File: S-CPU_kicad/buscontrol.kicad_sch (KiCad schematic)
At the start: 123 parts, among them U6 MUX, U8 MUX

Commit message: Fix ERC errors in schematics.
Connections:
- removed net 65816_?: LBOQ.3, MAWW.3, U6.4, U8.4
- net wIAYI renamed wIAYI_~{RST}
- net wJBDJ renamed CPU_~{RST}
- new net 65816_IN0: LBOQ.3
- new net 65816_IN1: MAWW.3
- new net 65816_PHI2: U8.4
- new net 65816_~{RST}: U6.4
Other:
- title: SNES S-CPU Schematics  -> Reverse Engineered SNES S-CPU Schematics 

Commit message: Big rework on the hierachical sheet to make thigs a bit clearer. PDF exported for Rev 0.1.
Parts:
- removed DCEG, FBSI: TRI_INV_IF2, symbol Ricoh_Cells:TRI_INV_IF2
- removed GBEG, IARF: OR_3, symbol Ricoh_Cells:OR_3
- removed HAKW, IBEP, JBDJ, JBQK, MBSK: BUF, symbol Ricoh_Cells:BUF
- removed HALC, HBCT, HBGA, IAQU, IBGG, KBVA, LBOQ, MAWW: OR_2, symbol Ricoh_Cells:OR_2
- removed HAMT, LBXR: D_LATCH_A2, symbol Ricoh_Cells:D_LATCH_A2
- removed HANA, HAZL, HBQJ, IAQS, IBNJ, JAXB, JBDE, LBWH, MBUB, ZOZP: INVERTER_A, symbol Ricoh_Cells:INVERTER_A
- removed HBCA, HBEP: TRI_INV_IF0, symbol Ricoh_Cells:TRI_INV_IF0
- removed IAQD, IAQV, JAXC, ROLZ: AND_2, symbol Ricoh_Cells:AND_2
- removed IARB, IOAW: TRI_BUF_IF0, symbol Ricoh_Cells:TRI_BUF_IF0
- removed JBHT: DFFR_A, symbol Ricoh_Cells:DFFR_A
- removed JBNA: OAI_112, symbol Ricoh_Cells:OAI_112
- removed JBND, JBPY, KBUP, ROMA: NAND_2, symbol Ricoh_Cells:NAND_2
- removed MBUP: AOI_22, symbol Ricoh_Cells:AOI_22
- removed RDY: IBUF, symbol Ricoh_Cells:IBUF
- removed U6, U8: MUX, symbol Ricoh_Cells:MUX
- removed VDA, VPA: IOBUF_B, symbol Ricoh_Cells:IOBUF_B
- OEFL, OEGK, OEKJ, OEOU, OEUB, OFAD, OFUH, OGBZ: value D_LATCH_A -> D_LATCH_A2; symbol Ricoh_Cells:D_LATCH_A -> Ricoh_Cells:D_LATCH_A2
- renumbered D7 to D0, D7 to D1, D7 to D2, D7 to D3, D7 to D4, D7 to D5, D7 to D6, AAXI1 to OEAP, ABVA2 to OECW, AAXI1 to OEFO, ABVA2 to OEGF, AAXI1 to OEGU, ABVA2 to OEJI, AAXI1 to OEMF, ABVA2 to OEOJ, AAXI1 to OEOY, ABVA2 to OEQL, AAXI1 to OEXG, ABVA2 to OEZO, AAXI1 to OFJV, ABVA2 to OFUA, AAXI1 to OFWO, ABVA2 to OGZF
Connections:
- net D0: now also OFXA.3 (D); no longer OFXA.2 (D)
- net D1: now also OFQH.3 (D); no longer OFQH.2 (D)
- net D2: now also OEYB.3 (D); no longer OEYB.2 (D)
- net D3: now also OEPS.3 (D); no longer OEPS.2 (D)
- net D4: now also OENU.3 (D); no longer OENU.2 (D)
- net D5: now also OEHW.3 (D); no longer OEHW.2 (D)
- net D6: now also OEFW.3 (D); no longer OEFW.2 (D)
- net D7: now also OEBY.3 (D); no longer OEBY.2 (D)
- net DATABUS_LATCH: no longer OEBY.3 (ENA), OEFL.3 (ENA), OEFW.3 (ENA), OEGK.3 (ENA), OEHW.3 (ENA), OEKJ.3 (ENA), OENU.3 (ENA), OEOU.3 (ENA), OEPS.3 (ENA), OEUB.3 (ENA), OEYB.3 (ENA), OFAD.3 (ENA), OFQH.3 (ENA), OFUH.3 (ENA), OFXA.3 (ENA), OGBZ.3 (ENA)
- net IN_D0: now also OGBZ.3 (D); no longer OGBZ.2 (D)
- net IN_D1: now also OFUH.3 (D); no longer OFUH.2 (D)
- net IN_D2: now also OFAD.3 (D); no longer OFAD.2 (D)
- net IN_D3: now also OEUB.3 (D); no longer OEUB.2 (D)
- net IN_D4: now also OEOU.3 (D); no longer OEOU.2 (D)
- net IN_D5: now also OEKJ.3 (D); no longer OEKJ.2 (D)
- net IN_D6: now also OEGK.3 (D); no longer OEGK.2 (D)
- net IN_D7: now also OEFL.3 (D); no longer OEFL.2 (D)
- net at OEQL.1 (IN), OEQL.3 (IN): now also OEUB.6 (~{Q}); no longer OEUB.5 (~{Q})
- net at OGZF.1 (IN), OGZF.3 (IN): now also OGBZ.6 (~{Q}); no longer OGBZ.5 (~{Q})
- net at OEJI.1 (IN), OEJI.3 (IN): now also OEKJ.6 (~{Q}); no longer OEKJ.5 (~{Q})
- net at OEGF.1 (IN), OEGF.3 (IN): now also OEGK.6 (~{Q}); no longer OEGK.5 (~{Q})
- net at OEGU.2: now also OEHW.5 (Q); no longer OEHW.4 (Q)
- net at OFWO.2: now also OFXA.5 (Q); no longer OFXA.4 (Q)
- net at OEXG.2: now also OEYB.5 (Q); no longer OEYB.4 (Q)
- net at OFJV.2: now also OFQH.5 (Q); no longer OFQH.4 (Q)
- net at OEOJ.1 (IN), OEOJ.3 (IN): now also OEOU.6 (~{Q}); no longer OEOU.5 (~{Q})
- net at OECW.1 (IN), OECW.3 (IN): now also OEFL.6 (~{Q}); no longer OEFL.5 (~{Q})
- net at OEOY.2: now also OEPS.5 (Q); no longer OEPS.4 (Q)
- net at OEFO.2: now also OEFW.5 (Q); no longer OEFW.4 (Q)
- net at OEMF.2: now also OENU.5 (Q); no longer OENU.4 (Q)
- net at OEAP.2: now also OEBY.5 (Q); no longer OEBY.4 (Q)
- net at OFUA.1 (IN), OFUA.3 (IN): now also OFUH.6 (~{Q}); no longer OFUH.5 (~{Q})
- net at OEZO.1 (IN), OEZO.3 (IN): now also OFAD.6 (~{Q}); no longer OFAD.5 (~{Q})
- net wOCOG_~{MODE7} renamed ~{MODE7}
- no-connect marks 9 -> 16
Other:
- note added: "DATA Bus is DOUT from CPU when one of the following conditions are met: - DMA is on and CPU_REG_RD = '1' and DMA_B->A = '0' and HDMA_TABLE_RD = '0' and ~{RDY} = '0' - DMA is off and ((R~{W} = '0' and SYSCLK = '1' and ~{RDY} = '0') or (CPU_REG_RD = '1' and ~{RDY} = '1')) ACLK is used instead of SYSCLK but it is an inverted version of it. DATA Bus is DIN to CPU when one of the following conditions 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"
- note removed: "Cells in DMA section but not connected. Change of design or test in early prototypes?"
- note removed: "Disconnects 65816 in MODE7, in MODE1 when RDY is low and during DMA"
- note removed: "IARF Goes low during internal CPU cycles VDA and VPA are low and DMA is not running"
- note removed: "JBNA = JBQK set to '1' when in MODE2-3, in MODE7, in MODE1 + RDY = 0 or DMA is OFF"
- note removed: "Low when RDY = 0 in mode 1 or when DMA is on in mode 4-6"
- note removed: "Open-bus behaviour somehow linked to DIN data getting the latched and taking over tri-stated D-bus bits."
- moved on the sheet: LCLR, LCQZ

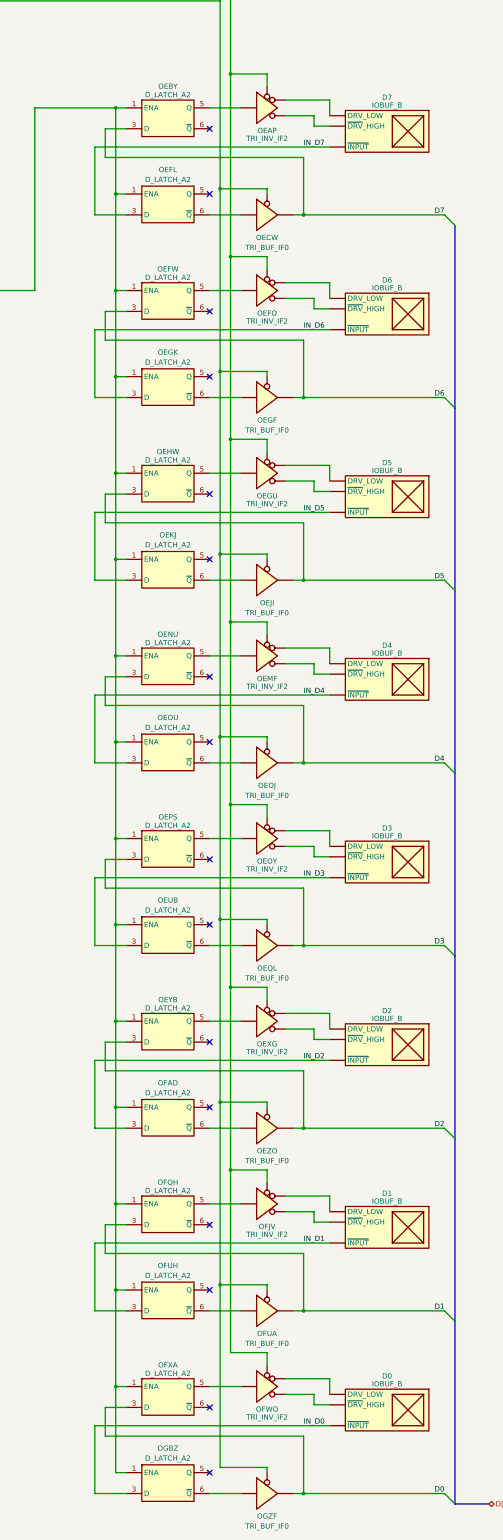
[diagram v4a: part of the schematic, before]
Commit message: Fixed VAWR which should have been an SR DFF (to fix issue #3 raised in github)
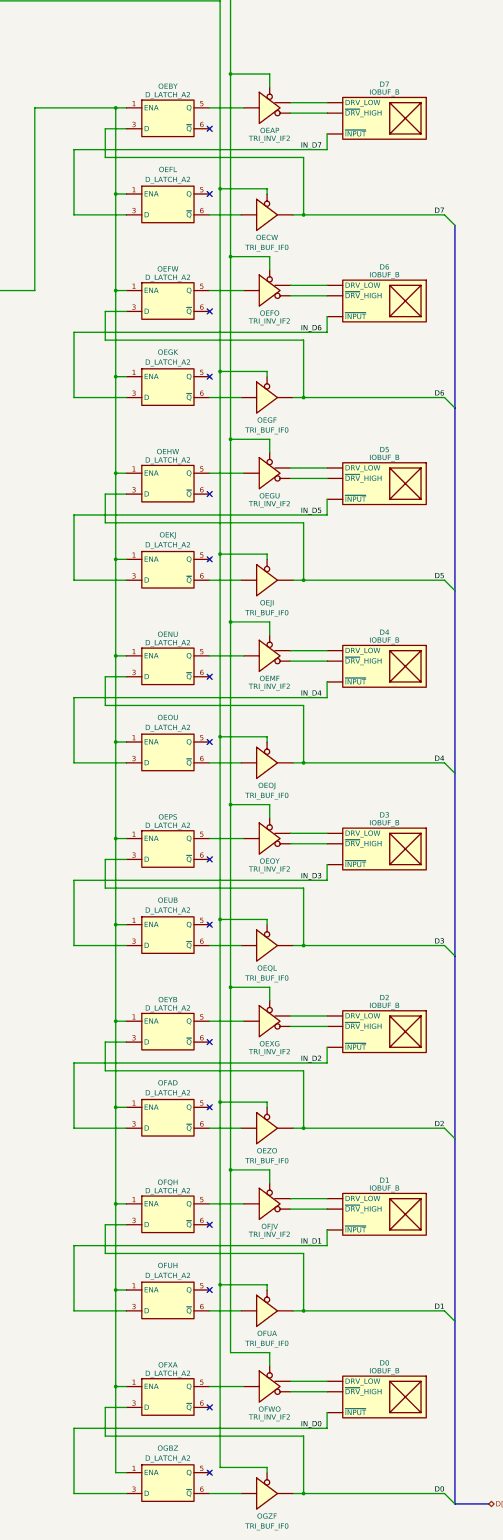
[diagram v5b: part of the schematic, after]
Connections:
- net at D3.4 (~{DRV}_HIGH): now also OEOY.4; no longer OEOY.3
- net at D6.4 (~{DRV}_HIGH): now also OEFO.4; no longer OEFO.3
- net at D0.4 (~{DRV}_HIGH): now also OFWO.4; no longer OFWO.3
- net at D1.4 (~{DRV}_HIGH): now also OFJV.4; no longer OFJV.3
- net at D7.4 (~{DRV}_HIGH): now also OEAP.4; no longer OEAP.3
- net at D2.4 (~{DRV}_HIGH): now also OEXG.4; no longer OEXG.3
- net at D4.4 (~{DRV}_HIGH): now also OEMF.4; no longer OEMF.3
- net at D5.4 (~{DRV}_HIGH): now also OEGU.4; no longer OEGU.3
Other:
- moved on the sheet: D0, D1, D2, D3, D4, D5, D6, D7
